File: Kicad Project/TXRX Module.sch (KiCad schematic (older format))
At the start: 0 parts

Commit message: test of git desktop and kicad
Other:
- note added: "Hello world"
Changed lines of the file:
@@
 $Descr A4 11693 8268
 encoding utf-8
-Sheet 1 4
+Sheet 3 4
 Title ""
 Date ""
@@
 Comment4 ""
 $EndDescr
+Text Notes 7200 5950 0    60   ~ 0
+Hello world
 $EndSCHEMATC

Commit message: interconnects
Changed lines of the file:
@@
 Text Notes 7200 5950 0    60   ~ 0
 Hello world
+Text HLabel 2350 2650 0    60   Input ~ 0
+transmit_in
+Text HLabel 2350 3050 0    60   Input ~ 0
+receive_out
 $EndSCHEMATC

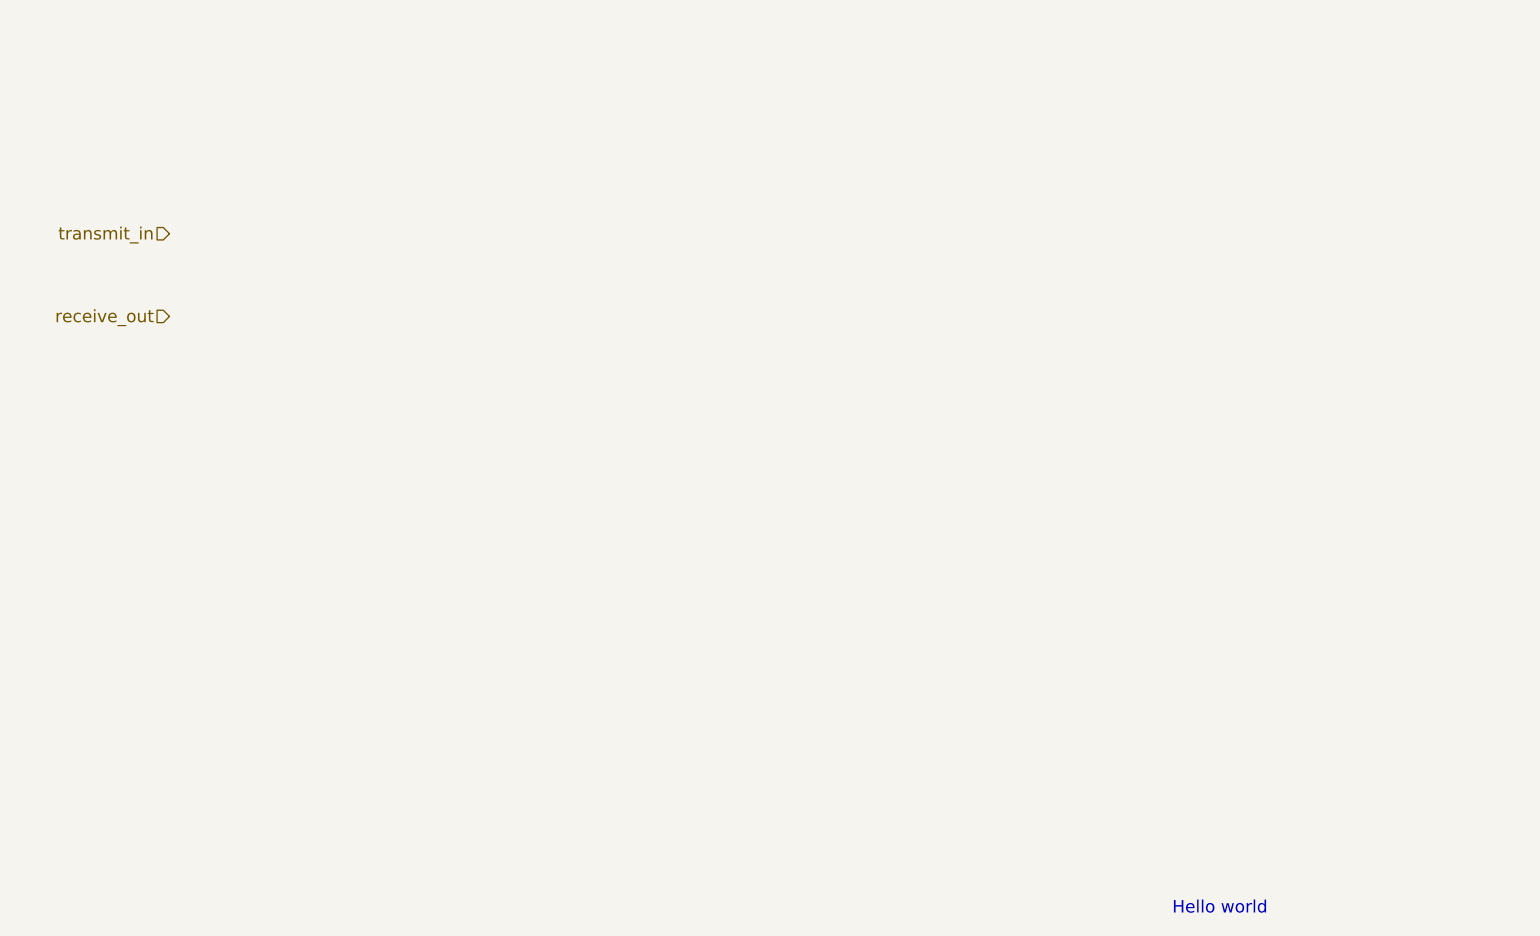
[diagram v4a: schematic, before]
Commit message: Updated TxRx module schematic
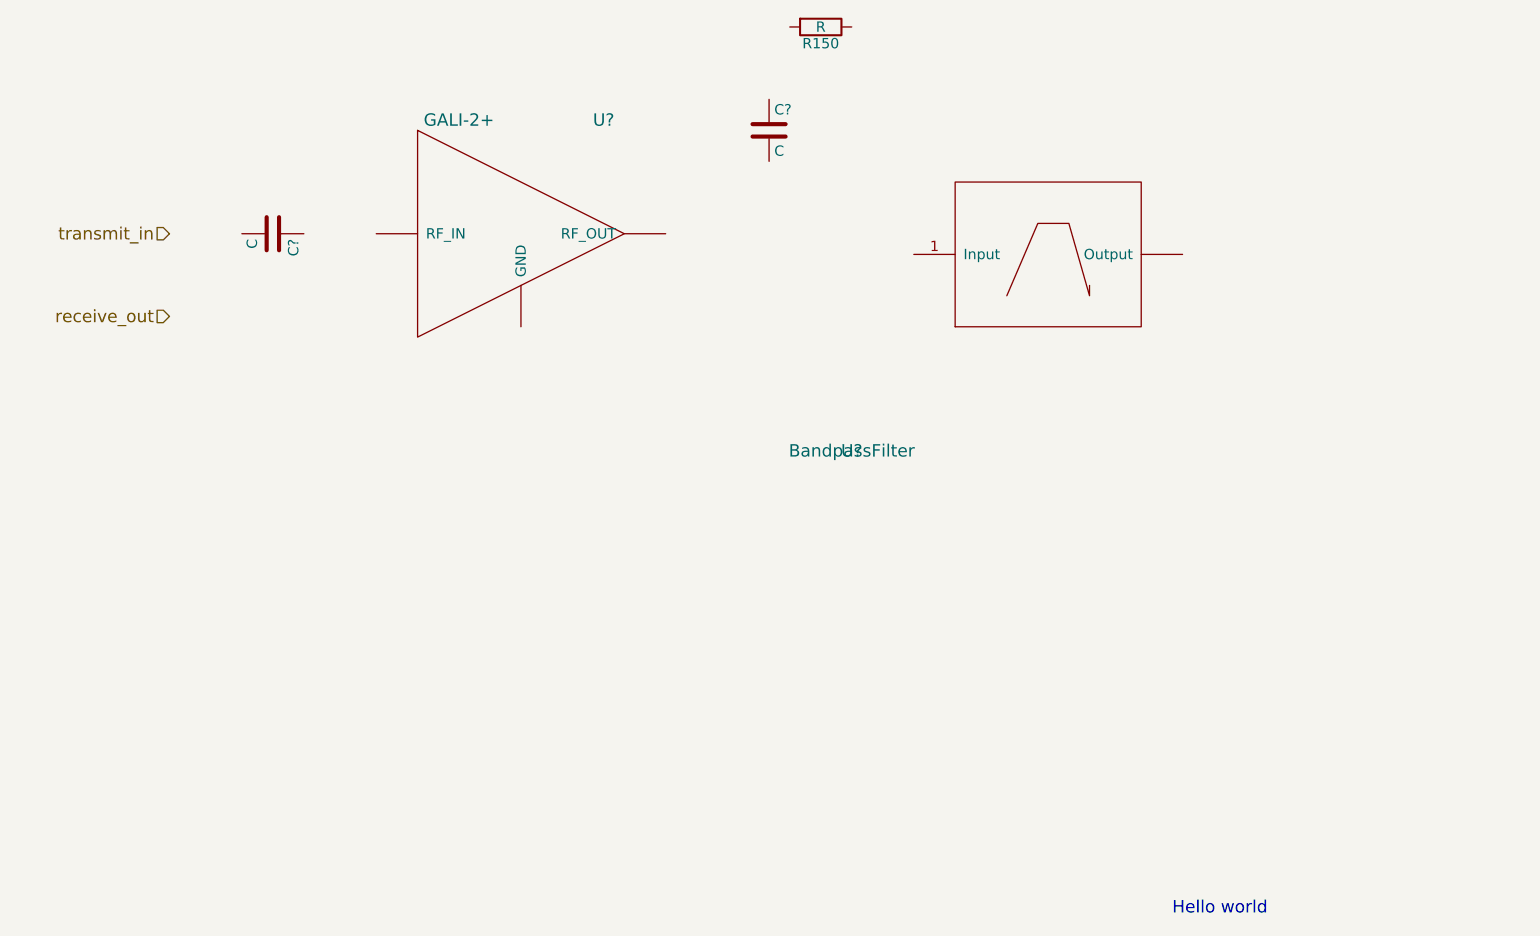
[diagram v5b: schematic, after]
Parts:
- added C? (x2): C, symbol C
- added R150: R, symbol R
- added U?: GALI-2+, symbol GALI-2+
- added U?: BandpassFilter, symbol BandpassFilter
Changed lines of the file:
@@
 Text HLabel 2350 3050 0    60   Input ~ 0
 receive_out
+$Comp
+L C C?
+U 1 1 59FF6B01
+P 2850 2650
+F 0 "C?" H 2875 2750 50  0000 L CNN
+F 1 "C" H 2875 2550 50  0000 L CNN
+F 2 "" H 2888 2500 50  0001 C CNN
+F 3 "" H 2850 2650 50  0001 C CNN
+	1    2850 2650
+	0    1    1    0
+$EndComp
+$Comp
+L C C?
+U 1 1 59FF6B4C
+P 5250 2150
+F 0 "C?" H 5275 2250 50  0000 L CNN
+F 1 "C" H 5275 2050 50  0000 L CNN
+F 2 "" H 5288 2000 50  0001 C CNN
+F 3 "" H 5250 2150 50  0001 C CNN
+	1    5250 2150
+	1    0    0    -1
+$EndComp
+$Comp
+L GALI-2+ U?
+U 1 1 59FF6FBF
+P 4050 2650
+F 0 "U?" H 4450 3200 60  0000 C CNN
+F 1 "GALI-2+" H 3750 3200 60  0000 C CNN
+F 2 "" H 4050 2650 60  0001 C CNN
+F 3 "" H 4050 2650 60  0001 C CNN
+	1    4050 2650
+	1    0    0    -1
+$EndComp
+$Comp
+L R R150
+U 1 1 59FF7053
+P 5500 1650
+F 0 "R150" V 5580 1650 50  0000 C CNN
+F 1 "R" V 5500 1650 50  0000 C CNN
+F 2 "" V 5430 1650 50  0001 C CNN
+F 3 "" H 5500 1650 50  0001 C CNN
+	1    5500 1650
+	0    1    1    0
+$EndComp
+$Comp
+L BandpassFilter U?
+U 1 1 59FF71CB
+P 5650 3700
+F 0 "U?" H 5650 3700 60  0000 C CNN
+F 1 "BandpassFilter" H 5650 3700 60  0000 C CNN
+F 2 "" H 5650 3700 60  0001 C CNN
+F 3 "" H 5650 3700 60  0001 C CNN
+	1    5650 3700
+	1    0    0    -1
+$EndComp
 $EndSCHEMATC

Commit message: added antennas and receive end
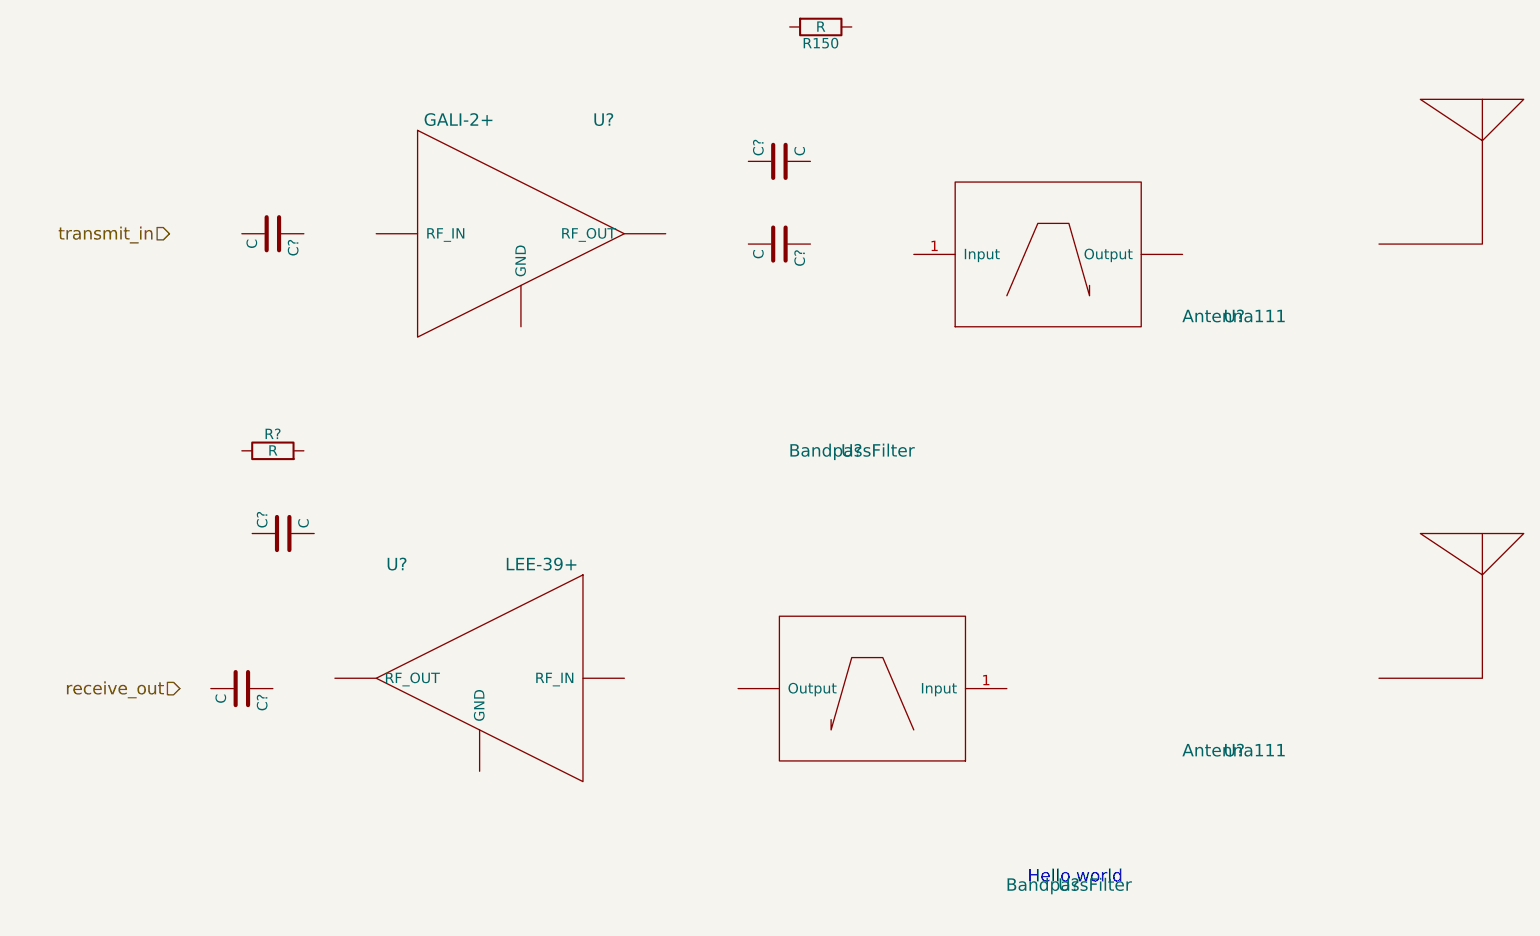
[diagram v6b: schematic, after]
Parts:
- added C? (x3): C, symbol C
- added R?: R, symbol R
- added U?: LEE-39+, symbol LEE-39+
- added U?: BandpassFilter, symbol BandpassFilter
- added U? (x2): Antenna111, symbol Antenna111
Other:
- moved on the sheet: C?
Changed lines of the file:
@@
 Comment4 ""
 $EndDescr
-Text Notes 7200 5950 0    60   ~ 0
+Text Notes 6500 5800 0    60   ~ 0
 Hello world
 Text HLabel 2350 2650 0    60   Input ~ 0
 transmit_in
-Text HLabel 2350 3050 0    60   Input ~ 0
+Text HLabel 2400 4850 0    60   Input ~ 0
 receive_out
 $Comp
@@
 L C C?
 U 1 1 59FF6B4C
-P 5250 2150
-F 0 "C?" H 5275 2250 50  0000 L CNN
-F 1 "C" H 5275 2050 50  0000 L CNN
-F 2 "" H 5288 2000 50  0001 C CNN
-F 3 "" H 5250 2150 50  0001 C CNN
-	1    5250 2150
-	1    0    0    -1
+P 5300 2300
+F 0 "C?" H 5325 2400 50  0000 L CNN
+F 1 "C" H 5325 2200 50  0000 L CNN
+F 2 "" H 5338 2150 50  0001 C CNN
+F 3 "" H 5300 2300 50  0001 C CNN
+	1    5300 2300
+	0    -1   -1   0
 $EndComp
 $Comp
@@
 	1    0    0    -1
 $EndComp
+$Comp
+L LEE-39+ U?
+U 1 1 59FFC0B0
+P 3850 4800
+F 0 "U?" H 4250 5350 60  0000 C CNN
+F 1 "LEE-39+" H 3550 5350 60  0000 C CNN
+F 2 "" H 3850 4800 60  0001 C CNN
+F 3 "" H 3850 4800 60  0001 C CNN
+	1    3850 4800
+	-1   0    0    -1
+$EndComp
+$Comp
+L BandpassFilter U?
+U 1 1 59FFC13A
+P 6700 5800
+F 0 "U?" H 6700 5800 60  0000 C CNN
+F 1 "BandpassFilter" H 6700 5800 60  0000 C CNN
+F 2 "" H 6700 5800 60  0001 C CNN
+F 3 "" H 6700 5800 60  0001 C CNN
+	1    6700 5800
+	-1   0    0    -1
+$EndComp
+$Comp
+L R R?
+U 1 1 59FFC214
+P 2850 3700
+F 0 "R?" V 2930 3700 50  0000 C CNN
+F 1 "R" V 2850 3700 50  0000 C CNN
+F 2 "" V 2780 3700 50  0001 C CNN
+F 3 "" H 2850 3700 50  0001 C CNN
+	1    2850 3700
+	0    -1   -1   0
+$EndComp
+$Comp
+L C C?
+U 1 1 59FFC2C3
+P 2900 4100
+F 0 "C?" H 2925 4200 50  0000 L CNN
+F 1 "C" H 2925 4000 50  0000 L CNN
+F 2 "" H 2938 3950 50  0001 C CNN
+F 3 "" H 2900 4100 50  0001 C CNN
+	1    2900 4100
+	0    -1   -1   0
+$EndComp
+$Comp
+L C C?
+U 1 1 59FFC68E
+P 5300 2700
+F 0 "C?" H 5325 2800 50  0000 L CNN
+F 1 "C" H 5325 2600 50  0000 L CNN
+F 2 "" H 5338 2550 50  0001 C CNN
+F 3 "" H 5300 2700 50  0001 C CNN
+	1    5300 2700
+	0    1    1    0
+$EndComp
+$Comp
+L C C?
+U 1 1 59FFC719
+P 2700 4850
+F 0 "C?" H 2725 4950 50  0000 L CNN
+F 1 "C" H 2725 4750 50  0000 L CNN
+F 2 "" H 2738 4700 50  0001 C CNN
+F 3 "" H 2700 4850 50  0001 C CNN
+	1    2700 4850
+	0    1    1    0
+$EndComp
+$Comp
+L Antenna111 U?
+U 1 1 59FFCB61
+P 7500 3050
+F 0 "U?" H 7500 3050 60  0000 C CNN
+F 1 "Antenna111" H 7500 3050 60  0000 C CNN
+F 2 "" H 7500 3050 60  0001 C CNN
+F 3 "" H 7500 3050 60  0001 C CNN
+	1    7500 3050
+	1    0    0    -1
+$EndComp
+$Comp
+L Antenna111 U?
+U 1 1 59FFCBF8
+P 7500 5150
+F 0 "U?" H 7500 5150 60  0000 C CNN
+F 1 "Antenna111" H 7500 5150 60  0000 C CNN
+F 2 "" H 7500 5150 60  0001 C CNN
+F 3 "" H 7500 5150 60  0001 C CNN
+	1    7500 5150
+	1    0    0    -1
+$EndComp

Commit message: Connected stuffs and things
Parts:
- removed R?: R, symbol R
- added R? (x3): 75, symbol R
- R: renamed from R150; value R -> 75
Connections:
- net labels added: GND
- wire segments 0 -> 23
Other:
- moved on the sheet: C?, U?
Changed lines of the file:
@@
 L C C?
 U 1 1 59FF6B4C
-P 5300 2300
-F 0 "C?" H 5325 2400 50  0000 L CNN
-F 1 "C" H 5325 2200 50  0000 L CNN
-F 2 "" H 5338 2150 50  0001 C CNN
-F 3 "" H 5300 2300 50  0001 C CNN
-	1    5300 2300
+P 5300 2100
+F 0 "C?" H 5325 2200 50  0000 L CNN
+F 1 "C" H 5325 2000 50  0000 L CNN
+F 2 "" H 5338 1950 50  0001 C CNN
+F 3 "" H 5300 2100 50  0001 C CNN
+	1    5300 2100
 	0    -1   -1   0
 $EndComp
@@
 $EndComp
 $Comp
-L R R150
+L R R
 U 1 1 59FF7053
 P 5500 1650
-F 0 "R150" V 5580 1650 50  0000 C CNN
-F 1 "R" V 5500 1650 50  0000 C CNN
+F 0 "R" V 5580 1650 50  0000 C CNN
+F 1 "75" V 5500 1650 50  0000 C CNN
 F 2 "" V 5430 1650 50  0001 C CNN
 F 3 "" H 5500 1650 50  0001 C CNN
@@
 L BandpassFilter U?
 U 1 1 59FF71CB
-P 5650 3700
-F 0 "U?" H 5650 3700 60  0000 C CNN
-F 1 "BandpassFilter" H 5650 3700 60  0000 C CNN
-F 2 "" H 5650 3700 60  0001 C CNN
-F 3 "" H 5650 3700 60  0001 C CNN
-	1    5650 3700
+P 5650 3600
+F 0 "U?" H 5650 3600 60  0000 C CNN
+F 1 "BandpassFilter" H 5650 3600 60  0000 C CNN
+F 2 "" H 5650 3600 60  0001 C CNN
+F 3 "" H 5650 3600 60  0001 C CNN
+	1    5650 3600
 	1    0    0    -1
 $EndComp
@@
 L BandpassFilter U?
 U 1 1 59FFC13A
-P 6700 5800
-F 0 "U?" H 6700 5800 60  0000 C CNN
-F 1 "BandpassFilter" H 6700 5800 60  0000 C CNN
-F 2 "" H 6700 5800 60  0001 C CNN
-F 3 "" H 6700 5800 60  0001 C CNN
-	1    6700 5800
+P 6700 5750
+F 0 "U?" H 6700 5750 60  0000 C CNN
+F 1 "BandpassFilter" H 6700 5750 60  0000 C CNN
+F 2 "" H 6700 5750 60  0001 C CNN
+F 3 "" H 6700 5750 60  0001 C CNN
+	1    6700 5750
 	-1   0    0    -1
 $EndComp
 $Comp
-L R R?
-U 1 1 59FFC214
-P 2850 3700
-F 0 "R?" V 2930 3700 50  0000 C CNN
-F 1 "R" V 2850 3700 50  0000 C CNN
-F 2 "" V 2780 3700 50  0001 C CNN
-F 3 "" H 2850 3700 50  0001 C CNN
-	1    2850 3700
+L C C?
+U 1 1 59FFC2C3
+P 2650 4200
+F 0 "C?" H 2675 4300 50  0000 L CNN
+F 1 "C" H 2675 4100 50  0000 L CNN
+F 2 "" H 2688 4050 50  0001 C CNN
+F 3 "" H 2650 4200 50  0001 C CNN
+	1    2650 4200
 	0    -1   -1   0
 $EndComp
 $Comp
 L C C?
-U 1 1 59FFC2C3
-P 2900 4100
-F 0 "C?" H 2925 4200 50  0000 L CNN
-F 1 "C" H 2925 4000 50  0000 L CNN
-F 2 "" H 2938 3950 50  0001 C CNN
-F 3 "" H 2900 4100 50  0001 C CNN
-	1    2900 4100
-	0    -1   -1   0
-$EndComp
-$Comp
-L C C?
 U 1 1 59FFC68E
-P 5300 2700
-F 0 "C?" H 5325 2800 50  0000 L CNN
-F 1 "C" H 5325 2600 50  0000 L CNN
-F 2 "" H 5338 2550 50  0001 C CNN
-F 3 "" H 5300 2700 50  0001 C CNN
-	1    5300 2700
+P 5300 2650
+F 0 "C?" H 5325 2750 50  0000 L CNN
+F 1 "C" H 5325 2550 50  0000 L CNN
+F 2 "" H 5338 2500 50  0001 C CNN
+F 3 "" H 5300 2650 50  0001 C CNN
+	1    5300 2650
 	0    1    1    0
 $EndComp
@@
 L C C?
 U 1 1 59FFC719
-P 2700 4850
-F 0 "C?" H 2725 4950 50  0000 L CNN
-F 1 "C" H 2725 4750 50  0000 L CNN
-F 2 "" H 2738 4700 50  0001 C CNN
-F 3 "" H 2700 4850 50  0001 C CNN
-	1    2700 4850
+P 2700 4800
+F 0 "C?" H 2725 4900 50  0000 L CNN
+F 1 "C" H 2725 4700 50  0000 L CNN
+F 2 "" H 2738 4650 50  0001 C CNN
+F 3 "" H 2700 4800 50  0001 C CNN
+	1    2700 4800
 	0    1    1    0
 $EndComp
@@
 L Antenna111 U?
 U 1 1 59FFCB61
-P 7500 3050
-F 0 "U?" H 7500 3050 60  0000 C CNN
-F 1 "Antenna111" H 7500 3050 60  0000 C CNN
-F 2 "" H 7500 3050 60  0001 C CNN
-F 3 "" H 7500 3050 60  0001 C CNN
-	1    7500 3050
+P 7400 3000
+F 0 "U?" H 7400 3000 60  0000 C CNN
+F 1 "Antenna111" H 7400 3000 60  0000 C CNN
+F 2 "" H 7400 3000 60  0001 C CNN
+F 3 "" H 7400 3000 60  0001 C CNN
+	1    7400 3000
 	1    0    0    -1
 $EndComp
@@
 	1    0    0    -1
 $EndComp
+$Comp
+L R R?
+U 1 1 59FFDD37
+P 4950 2450
+F 0 "R?" V 5030 2450 50  0000 C CNN
+F 1 "75" V 4950 2450 50  0000 C CNN
+F 2 "" V 4880 2450 50  0001 C CNN
+F 3 "" H 4950 2450 50  0001 C CNN
+	1    4950 2450
+	1    0    0    -1
+$EndComp
+Wire Wire Line
+	2350 2650 2700 2650
+Wire Wire Line
+	3000 2650 3350 2650
+Wire Wire Line
+	4750 2650 5150 2650
+Wire Wire Line
+	5450 2650 5950 2650
+Wire Wire Line
+	4950 2600 4950 2650
+Connection ~ 4950 2650
+Wire Wire Line
+	4950 1650 4950 2300
+Wire Wire Line
+	4950 2100 5150 2100
+Wire Wire Line
+	4950 1650 5350 1650
+Connection ~ 4950 2100
+Wire Wire Line
+	8100 2650 7250 2650
+$Comp
+L R R?
+U 1 1 59FFE442
+P 3450 3950
+F 0 "R?" V 3530 3950 50  0000 C CNN
+F 1 "75" V 3450 3950 50  0000 C CNN
+F 2 "" V 3380 3950 50  0001 C CNN
+F 3 "" H 3450 3950 50  0001 C CNN
+	1    3450 3950
+	0    -1   -1   0
+$EndComp
+$Comp
+L R R?
+U 1 1 59FFE542
+P 2950 4600
+F 0 "R?" V 3030 4600 50  0000 C CNN
+F 1 "75" V 2950 4600 50  0000 C CNN
+F 2 "" V 2880 4600 50  0001 C CNN
+F 3 "" H 2950 4600 50  0001 C CNN
+	1    2950 4600
+	-1   0    0    1
+$EndComp
+$Comp
+L GND #PWR?
+U 1 1 59FFE5A2
+P 2350 4350
+F 0 "#PWR?" H 2350 4100 50  0001 C CNN
+F 1 "GND" H 2350 4200 50  0000 C CNN
+F 2 "" H 2350 4350 50  0001 C CNN
+F 3 "" H 2350 4350 50  0001 C CNN
+	1    2350 4350
+	1    0    0    -1
+$EndComp
+$Comp
+L GND #PWR?
+U 1 1 59FFE5D4
+P 3850 5400
+F 0 "#PWR?" H 3850 5150 50  0001 C CNN
+F 1 "GND" H 3850 5250 50  0000 C CNN
+F 2 "" H 3850 5400 50  0001 C CNN
+F 3 "" H 3850 5400 50  0001 C CNN
+	1    3850 5400
+	1    0    0    -1
+$EndComp
+$Comp
+L GND #PWR?
+U 1 1 59FFE606
+P 4050 3200
+F 0 "#PWR?" H 4050 2950 50  0001 C CNN
+F 1 "GND" H 4050 3050 50  0000 C CNN
+F 2 "" H 4050 3200 50  0001 C CNN
+F 3 "" H 4050 3200 50  0001 C CNN
+	1    4050 3200
+	1    0    0    -1
+$EndComp
+$Comp
+L GND #PWR?
+U 1 1 59FFE638
+P 5450 2200
+F 0 "#PWR?" H 5450 1950 50  0001 C CNN
+F 1 "GND" H 5450 2050 50  0000 C CNN
+F 2 "" H 5450 2200 50  0001 C CNN
+F 3 "" H 5450 2200 50  0001 C CNN
+	1    5450 2200
+	1    0    0    -1
+$EndComp
+Wire Wire Line
+	8200 4800 6400 4800
+Wire Wire Line
+	5100 4800 4550 4800
+Wire Wire Line
+	3150 4800 2850 4800
+Wire Wire Line
+	2950 4750 2950 4800
+Connection ~ 2950 4800
+Wire Wire Line
+	2950 4450 2950 3950
+Wire Wire Line
+	2950 3950 3300 3950
+Wire Wire Line
+	2800 4200 2950 4200
+Connection ~ 2950 4200
+Wire Wire Line
+	2500 4200 2350 4200
+Wire Wire Line
+	2350 4200 2350 4350
+Wire Wire Line
+	3850 5250 3850 5400
+Wire Wire Line
+	5450 2100 5450 2200
+Wire Wire Line
+	4050 3100 4050 3200
+Wire Wire Line
+	2550 4800 2400 4800
+Wire Wire Line
+	2400 4800 2400 4850
 $EndSCHEMATC
